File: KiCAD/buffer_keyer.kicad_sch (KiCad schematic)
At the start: 65 parts, among them J1 Conn_01x02_Pin, J13 Conn_01x05, J2 Conn_01x02_Pin, J3 Conn_01x02_Pin, T1 2N3906, T2 2N3906, U3 MC1496, U4 MCP4921, U6 LM7171xIN, U7 LM7171xIN, U8 MCP4728

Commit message: kicad: convert hierarchical labels to globals (Path A) + unify _OUT/_IN pairs
- 58 hierarchical_label -> global_label conversions across the six active
  sheets. Standard KiCad 10 global_label form with fields_autoplaced +
  Intersheetrefs property.
- Stripped 36 vestigial sheet pins, 28 stitching wires, 2 junctions, 4
  labels from the root sheet. Sheet blocks remain; each is now a pure
  container with globals doing the cross-sheet connectivity by name.
- Renamed three OUT/IN pairs to unified names so same-name globals
  auto-connect:
    GRID_CTL_A_OUT + GRID_CTL_A_IN -> GRID_CTL_A
    GRID_CTL_B_OUT + GRID_CTL_B_IN -> GRID_CTL_B
    RAW_RF_OUT     + RAW_RF_IN     -> RAW_RF
- tools/convert_hier_to_global.py and tools/strip_root_stitching.py:
  reusable if we ever need to redo this.
- Documentation/punch_list_7-6-26.txt: mark B1a-e, L1, L2 resolved; add
  M6 (cosmetic) about GRID_CTL_A's label-at-pin-origin idiom; correct
  the earlier GRID_CTL_A false positive with the verified chain
  MCP4728 U8 VC -> R_PADA -> OPA454 U5 IN+ + Q3 drain.

Co-Authored-By: Claude Opus 4.7 (1M context) <noreply@anthropic.com>
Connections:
- net GRID_CTL_A_OUT renamed GRID_CTL_A
- net GRID_CTL_B_OUT renamed GRID_CTL_B
- net RAW_RF_IN renamed RAW_RF

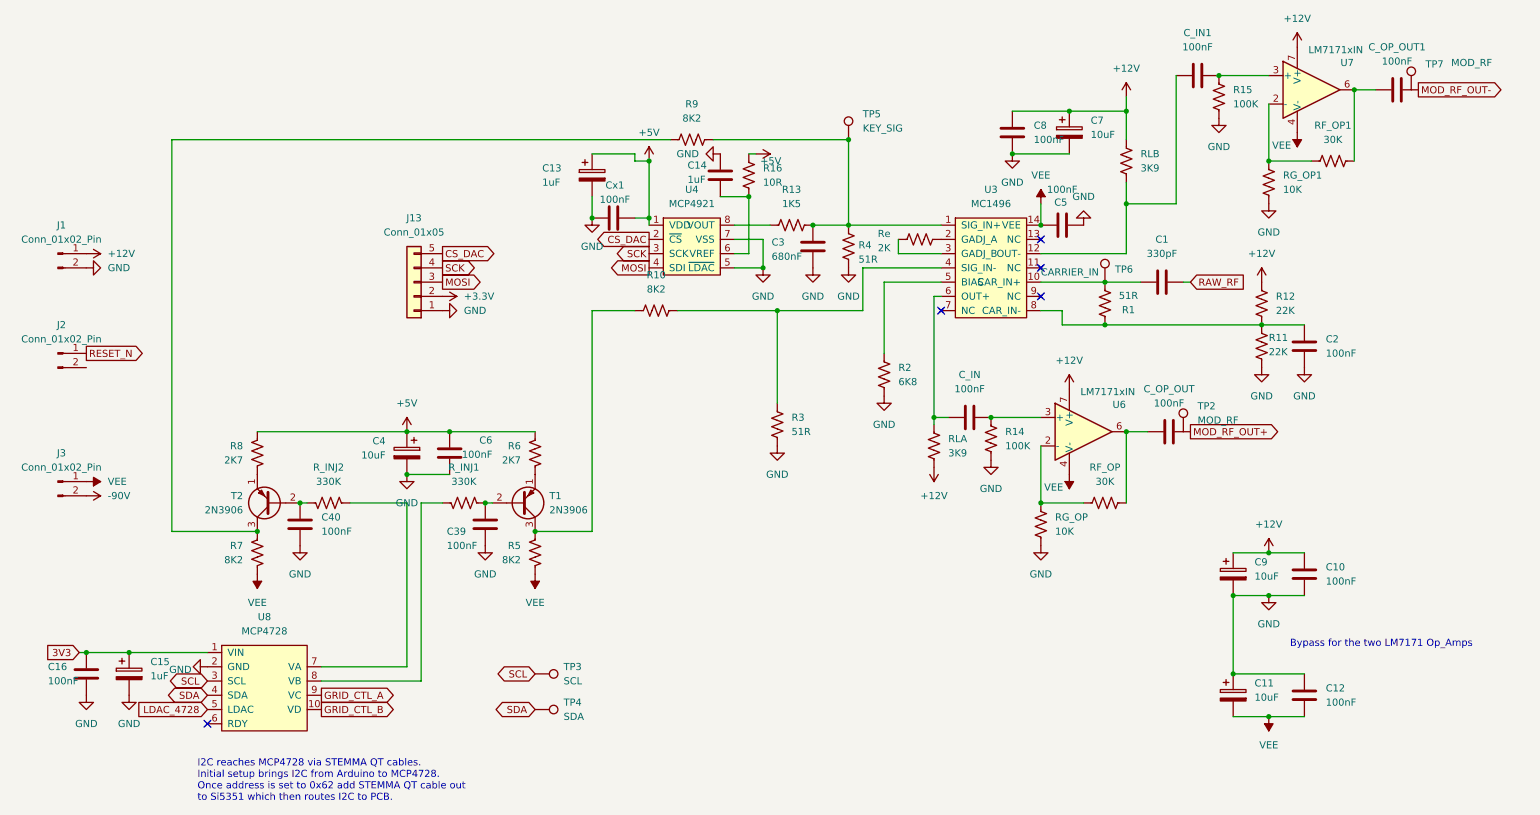
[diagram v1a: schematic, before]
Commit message: kicad: fill 9 remaining footprints across active sheets
- arduino: R30 470K (R_Axial_DIN0207 horizontal), C41 1uF (rect L7.2mm),
  C42 100nF (disc D5mm P5mm), C43 10uF (radial polarized D5mm P2mm)
- bias: J11 (GRID_BIAS), J12 (CATHODE_SENSE), J14 -- all PinHeader_1x02
  vertical THT
- buffer_keyer: J13 -- PinHeader_1x05 vertical THT
- interface: J15 -- PinHeader_1x03 vertical THT

C41/C42/C43 filled by re-running tools/assign_cap_footprints.py which
already had the intended mappings. R30 and the connectors done by hand
via a one-off script.

Only U2 (Metro) remains footprint-less, intentionally off-PCB.

Punch list updates for today's ERC pass + user's schematic edits:
- B3 (footprints) resolved.
- B4d/B4e (TP2/TP7 to MOD_RF+/-) resolved -- user verified junction dots
  + wires in KiCad. TP3 = SCL is intentional (I2C debug probe access).
- M5 (TX_LED) previously resolved -- LED wired in parallel with T/R
  relay coil, no Metro GPIO needed.
- B2 (paddle) rewritten for the actual design: J10 = 2-conductor 1/4"
  phone plug, tip -> Metro D5, sleeve -> GND.

vfo.kicad_sch diff is KiCad's own canonicalization of Intersheetrefs
property (show_name/do_not_autoplace fields shuffled) from opening +
saving; contents equivalent.

Co-Authored-By: Claude Opus 4.7 (1M context) <noreply@anthropic.com>
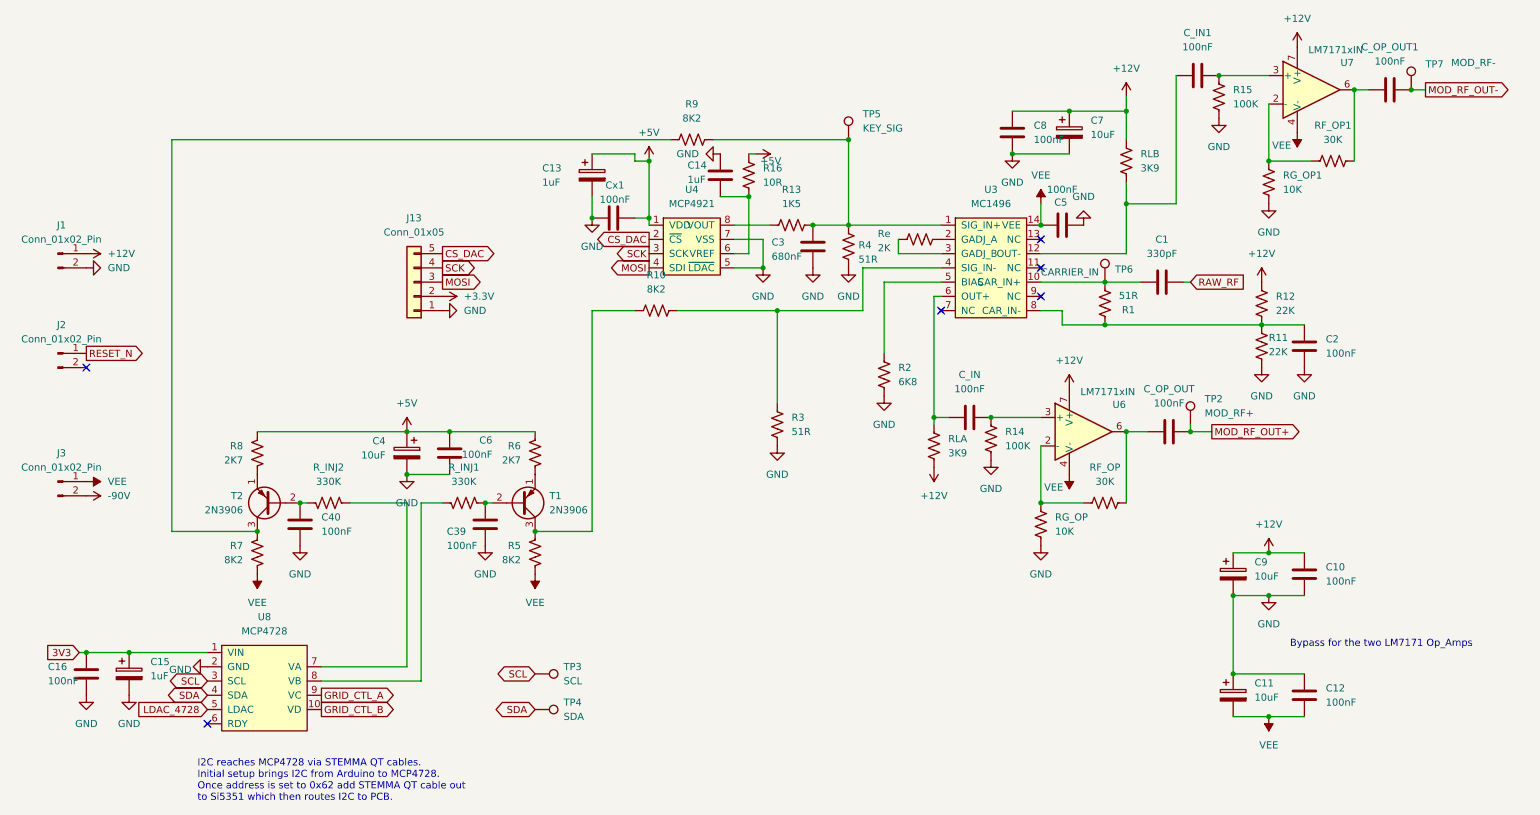
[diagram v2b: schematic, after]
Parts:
- J13: footprint (none) -> Connector_PinHeader_2.54mm:PinHeader_1x05_P2.54mm_Vertical
- TP2: value MOD_RF -> MOD_RF+
- TP7: value MOD_RF -> MOD_RF-
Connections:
- net MOD_RF_OUT+: now also TP2.1
- net MOD_RF_OUT-: now also TP7.1
- no-connect marks 5 -> 6
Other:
- moved on the sheet: C_OP_OUT1, TP2
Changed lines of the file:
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@@
 	)
 	(junction
+		(at 252.73 31.75)
+		(diameter 0)
+		(color 0 0 0 0)
+	)
+	(junction
 		(at 106.68 110.49)
 		(diameter 0)
@@
 	)
 	(junction
-		(at 252.73 31.75)
+		(at 223.52 92.71)
 		(diameter 0)
 		(color 0 0 0 0)
@@
 	)
 	(junction
+		(at 262.89 31.75)
+		(diameter 0)
+		(color 0 0 0 0)
+	)
+	(junction
 		(at 91.44 92.71)
 		(diameter 0)
@@
 	)
 	(no_connect
+		(at 26.67 81.28)
+	)
+	(no_connect
 		(at 196.85 63.5)
 	)
@@
 	(wire
 		(pts
-			(xy 252.73 31.75) (xy 256.54 31.75)
+			(xy 252.73 31.75) (xy 255.27 31.75)
 		)
 		(stroke
@@
 	(wire
 		(pts
+			(xy 227.33 92.71) (xy 223.52 92.71)
+		)
+		(stroke
+			(width 0)
+			(type default)
+		)
+	)
+	(wire
+		(pts
 			(xy 132.08 71.12) (xy 149.86 71.12)
 		)
@@
 	(wire
 		(pts
+			(xy 262.89 31.75) (xy 265.43 31.75)
+		)
+		(stroke
+			(width 0)
+			(type default)
+		)
+	)
+	(wire
+		(pts
 			(xy 212.09 33.02) (xy 212.09 35.56)
 		)
@@
 	(wire
 		(pts
+			(xy 223.52 91.44) (xy 223.52 92.71)
+		)
+		(stroke
+			(width 0)
+			(type default)
+		)
+	)
+	(wire
+		(pts
 			(xy 149.86 71.12) (xy 149.86 87.63)
 		)
@@
 		(property "Intersheetrefs" "${INTERSHEET_REFS}"
 			(at 68.58 139.7 0)
+			(hide yes)
+			(show_name no)
+			(do_not_autoplace no)
 			(effects
 				(font
 					(size 1.27 1.27)
 				)
-				(hide yes)
 			)
 		)
@@
 		(property "Intersheetrefs" "${INTERSHEET_REFS}"
 			(at 25.4 132.08 0)
+			(hide yes)
+			(show_name no)
+			(do_not_autoplace no)
 			(effects
 				(font
 					(size 1.27 1.27)
 				)
-				(hide yes)
 			)
 		)
@@
 	(global_label "MOD_RF_OUT+"
 		(shape output)
-		(at 223.52 92.71 0)
+		(at 227.33 92.71 0)
 		(fields_autoplaced yes)
 		(effects
@@
 		)
 		(property "Intersheetrefs" "${INTERSHEET_REFS}"
-			(at 223.52 92.71 0)
+			(at 227.33 92.71 0)
+			(hide yes)
+			(show_name no)
+			(do_not_autoplace no)
 			(effects
 				(font
 					(size 1.27 1.27)
 				)
-				(hide yes)
 			)
 		)
@@
 		(property "Intersheetrefs" "${INTERSHEET_REFS}"
 			(at 106.68 142.24 0)
+			(hide yes)
+			(show_name no)
+			(do_not_autoplace no)
 			(effects
 				(font
 					(size 1.27 1.27)
 				)
-				(hide yes)
 			)
 		)
@@
 		(property "Intersheetrefs" "${INTERSHEET_REFS}"
 			(at 48.26 137.16 0)
+			(hide yes)
+			(show_name no)
+			(do_not_autoplace no)
 			(effects
 				(font
 					(size 1.27 1.27)
 				)
-				(hide yes)
 			)
 		)
@@
 		(property "Intersheetrefs" "${INTERSHEET_REFS}"
 			(at 127 60.96 0)
+			(hide yes)
+			(show_name no)
+			(do_not_autoplace no)
 			(effects
 				(font
 					(size 1.27 1.27)
 				)
-				(hide yes)
 			)
 		)
@@
 	(global_label "MOD_RF_OUT-"
 		(shape output)
-		(at 264.16 31.75 0)
+		(at 265.43 31.75 0)
 		(fields_autoplaced yes)
 		(effects
@@
 		)
 		(property "Intersheetrefs" "${INTERSHEET_REFS}"
-			(at 264.16 31.75 0)
+			(at 265.43 31.75 0)
+			(hide yes)
+			(show_name no)
+			(do_not_autoplace no)
 			(effects
 				(font
 					(size 1.27 1.27)
 				)
-				(hide yes)
 			)
 		)
@@
 		(property "Intersheetrefs" "${INTERSHEET_REFS}"
 			(at 90.17 63.5 0)
+			(hide yes)
+			(show_name no)
+			(do_not_autoplace no)
 			(effects
 				(font
 					(size 1.27 1.27)
 				)
-				(hide yes)
 			)
 		)
@@
 		(property "Intersheetrefs" "${INTERSHEET_REFS}"
 			(at 106.68 135.89 0)
+			(hide yes)
+			(show_name no)
+			(do_not_autoplace no)
 			(effects
 				(font
 					(size 1.27 1.27)
 				)
-				(hide yes)
 			)
 		)
@@
 		(property "Intersheetrefs" "${INTERSHEET_REFS}"
 			(at 26.67 78.74 0)
+			(hide yes)
+			(show_name no)
+			(do_not_autoplace no)
 			(effects
 				(font
 					(size 1.27 1.27)
 				)
-				(hide yes)
 			)
 		)
@@
 		(property "Intersheetrefs" "${INTERSHEET_REFS}"
 			(at 68.58 142.24 0)
+			(hide yes)
+			(show_name no)
+			(do_not_autoplace no)
 			(effects
 				(font
 					(size 1.27 1.27)
 				)
-				(hide yes)
 			)
 		)
@@
 		(property "Intersheetrefs" "${INTERSHEET_REFS}"
 			(at 90.17 66.04 0)
+			(hide yes)
+			(show_name no)
+			(do_not_autoplace no)
 			(effects
 				(font
 					(size 1.27 1.27)
 				)
-				(hide yes)
 			)
 		)
@@
 		(property "Intersheetrefs" "${INTERSHEET_REFS}"
 			(at 90.17 60.96 0)
+			(hide yes)
+			(show_name no)
+			(do_not_autoplace no)
 			(effects
 				(font
 					(size 1.27 1.27)
 				)
-				(hide yes)
 			)
 		)
@@
 		(property "Intersheetrefs" "${INTERSHEET_REFS}"
 			(at 48.26 139.7 0)
+			(hide yes)
+			(show_name no)
+			(do_not_autoplace no)
 			(effects
 				(font
 					(size 1.27 1.27)
 				)
-				(hide yes)
 			)
 		)
@@
 		(property "Intersheetrefs" "${INTERSHEET_REFS}"
 			(at 223.52 66.04 0)
+			(hide yes)
+			(show_name no)
+			(do_not_autoplace no)
 			(effects
 				(font
 					(size 1.27 1.27)
 				)
-				(hide yes)
 			)
 		)
@@
 		(property "Intersheetrefs" "${INTERSHEET_REFS}"
 			(at 127 63.5 0)
+			(hide yes)
+			(show_name no)
+			(do_not_autoplace no)
 			(effects
 				(font
 					(size 1.27 1.27)
 				)
-				(hide yes)
 			)
 		)
@@
 		(property "Intersheetrefs" "${INTERSHEET_REFS}"
 			(at 127 58.42 0)
+			(hide yes)
+			(show_name no)
+			(do_not_autoplace no)
 			(effects
 				(font
 					(size 1.27 1.27)
 				)
-				(hide yes)
 			)
 		)
@@
 		(property "Intersheetrefs" "${INTERSHEET_REFS}"
 			(at 48.26 142.24 0)
+			(hide yes)
+			(show_name no)
+			(do_not_autoplace no)
 			(effects
 				(font
 					(size 1.27 1.27)
 				)
-				(hide yes)
 			)
 		)
@@
 			)
 		)
-		(property "Footprint" ""
+		(property "Footprint" "Connector_PinHeader_2.54mm:PinHeader_1x05_P2.54mm_Vertical"
 			(at 85.09 66.04 0)
 			(hide yes)
@@
 	(symbol
 		(lib_id "xmitter:xTP")
-		(at 222.25 92.71 0)
+		(at 223.52 91.44 0)
 		(unit 1)
 		(body_style 1)
@@
 		(fields_autoplaced yes)
 		(property "Reference" "TP2"
-			(at 224.79 88.1379 0)
+			(at 226.06 86.8679 0)
 			(show_name no)
 			(do_not_autoplace no)
@@
 			)
 		)
-		(property "Value" "MOD_RF"
-			(at 224.79 90.6779 0)
+		(property "Value" "MOD_RF+"
+			(at 226.06 89.4079 0)
 			(show_name no)
 			(do_not_autoplace no)
@@
 		)
 		(property "Footprint" "Connector_PinHeader_2.54mm:PinHeader_1x01_P2.54mm_Vertical"
-			(at 227.33 92.71 0)
+			(at 228.6 91.44 0)
 			(hide yes)
 			(show_name no)
@@
 		)
 		(property "Datasheet" ""
-			(at 227.33 92.71 0)
+			(at 228.6 91.44 0)
 			(hide yes)
 			(show_name no)
@@
 		)
 		(property "Description" "xmitter project test point on broken-off 0.1 inch square pin header; put signal name in Value field so it becomes silk on the PCB"
-			(at 222.25 92.71 0)
+			(at 223.52 91.44 0)
 			(hide yes)
 			(show_name no)
@@
 			)
 		)
-		(property "Value" "MOD_RF"
+		(property "Value" "MOD_RF-"
 			(at 270.002 26.924 0)
 			(show_name no)
@@
 	(symbol
 		(lib_id "Device:C")
-		(at 260.35 31.75 90)
+		(at 259.08 31.75 90)
 		(unit 1)
 		(body_style 1)
@@
 		(fields_autoplaced yes)
 		(property "Reference" "C_OP_OUT1"
-			(at 260.35 24.13 90)
+			(at 259.08 24.13 90)
 			(show_name no)
 			(do_not_autoplace no)
@@
 		)
 		(property "Value" "100nF"
-			(at 260.35 26.67 90)
+			(at 259.08 26.67 90)
 			(show_name no)
 			(do_not_autoplace no)
@@
 		)
 		(property "Footprint" "Capacitor_THT:C_Disc_D5.0mm_W2.5mm_P5.00mm"
-			(at 264.16 30.7848 0)
+			(at 262.89 30.7848 0)
 			(hide yes)
 			(show_name no)
@@
 		)
 		(property "Datasheet" ""
-			(at 260.35 31.75 0)
+			(at 259.08 31.75 0)
 			(hide yes)
 			(show_name no)
@@
 		)
 		(property "Description" "Unpolarized capacitor"
-			(at 260.35 31.75 0)
+			(at 259.08 31.75 0)
 			(hide yes)
 			(show_name no)

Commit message: kicad: PWR_FLAGs added, most +3.3V converted to 3V3, VFO renames + J2 NC
User work today:
- Placed PWR_FLAGs to silence "power_pin_not_driven" ERC errors for VEE,
  +12V, -90V rails (see B5a-B5f in the punch list)
- Converted 6 of 7 +3.3V power symbols to 3V3 global labels project-wide
  (one +3.3V remains on bias sheet, resolves next pass)
- VFO sheet: C_coup -> C_IN1, R6 -> RD1 (both were unannotated / duplicate
  ref designators; ERC B4a and B4b now resolved)
- buffer_keyer: J2 pin 2 gets a no_connect flag (B4c resolved); TP2 and
  TP7 electrically wired to MOD_RF_OUT+/- via junctions (B4d/e resolved)

Punch list updates:
- B3 (footprints) marked done
- B4a/b/c marked done
- M5 (TX LED) confirmed resolved (external LED across T/R relay coil)
- B2 (paddle) rewritten for the actual 2-conductor 1/4" plug scheme

Current ERC status: 61 errors, 0 warnings (from 74 + 2 originally).
Remaining real bugs: unannotated C_IN + duplicate C_IN1 on buffer_keyer,
misplaced #FLG04 on Metro's 3V3 pin, one leftover +3.3V on bias. Rest
are the known-non-issue plateau.

Co-Authored-By: Claude Opus 4.7 (1M context) <noreply@anthropic.com>
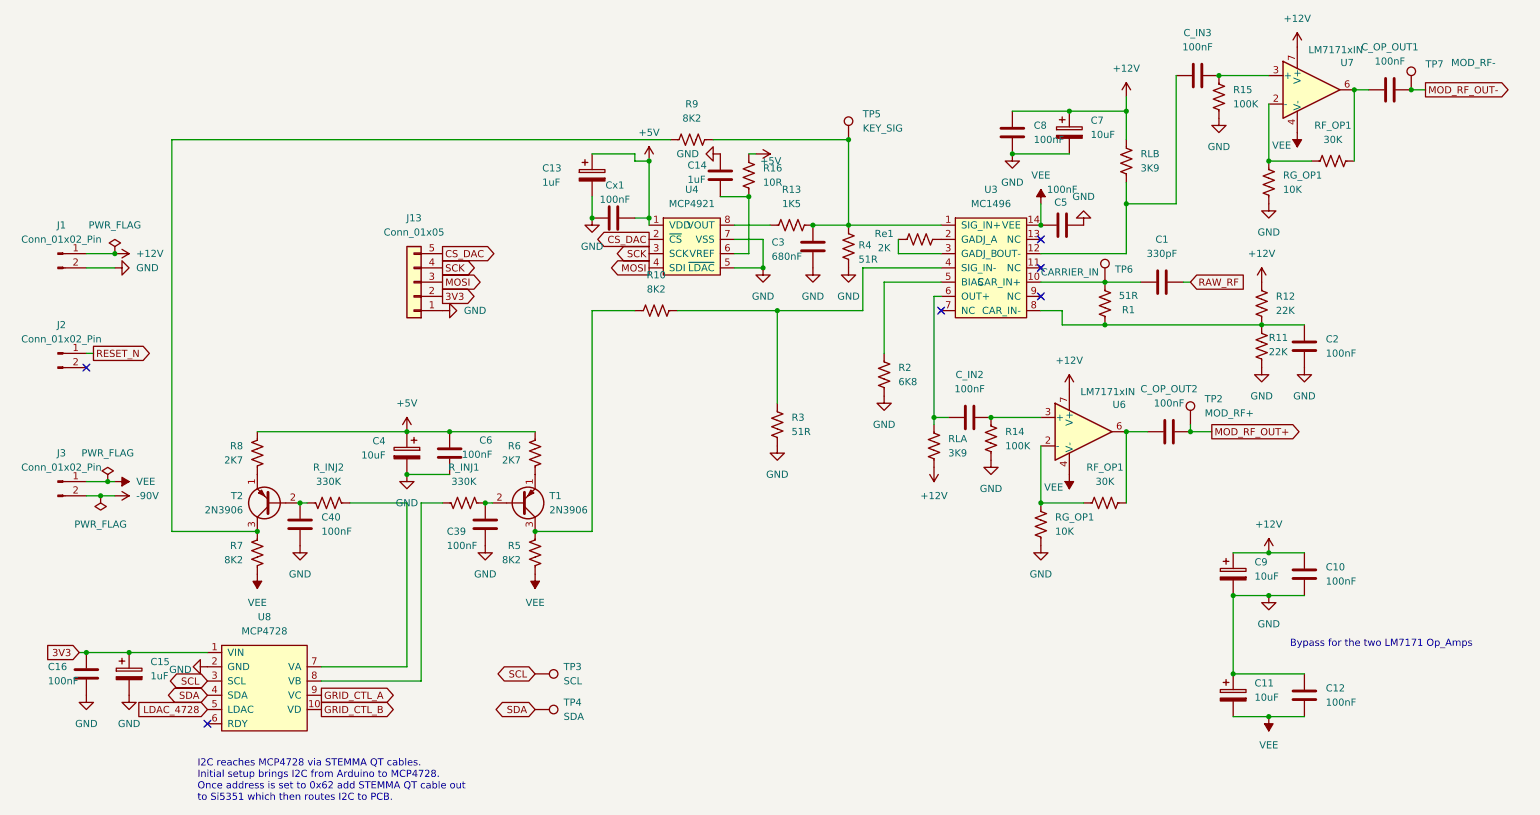
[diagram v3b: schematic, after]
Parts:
- renumbered C_IN to C_IN2, C_IN1 to C_IN3, C_OP_OUT to C_OP_OUT2, RF_OP to RF_OP1, RG_OP to RG_OP1, Re to Re1
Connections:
- net +3.3V is gone; now on net 3V3: J13.2 (Pin_2)
